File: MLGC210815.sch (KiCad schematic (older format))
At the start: 108 parts, among them J1 PinStrip_01x06_Male, J2 USB-B-04PFHTW, Q1 P-MOSFET_SI2315BDS-T1-E3, Q2 NPN_BC817, Q3 NPN_BC817, Q4 P-MOSFET_SI2315BDS-T1-E3, SW1 Switch-Tact_OMRON-B3F-3100, SW2 Switch-Tact_OMRON-B3F-3100, SW3 Switch-Tact_OMRON-B3F-3100, U1 PIC32MX170F256B-ISS, U2 OPA_MCP6V36T-E_OT, U3 LDO-MCP1700T-3302E_TT-Others, U4 SENSOR_BMA250E, U5 INTERFACE_FT230XS, U6 BATTERY_MCP73833-FCI_UN, U7 DISPLAY_REX012832FSPP3N01, Y1 Crystal_HC49SM_8MHz

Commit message: update
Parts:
- removed C14: Capacitator_0603_47nF_X7R, Passive:C_0603, symbol Passive:Capacitator_0603_47nF_X7R
- removed R16: Resistor_0603_4K70, Passive:R_0603, symbol Passive:Resistor_0603_4K70
- removed R17: Resistor_0603_9K10, Passive:R_0603, symbol Passive:Resistor_0603_9K10
- removed R18: Resistor_0603_10R0, Passive:R_0603, symbol Passive:Resistor_0603_10R0
- removed R44: Resistor_0603_0R00, Passive:R_0603, symbol Passive:Resistor_0603_0R00
- removed Y1: Crystal_HC49SM_8MHz, Passive:Crystal_SMD_HC49-SD, symbol Passive:Crystal_HC49SM_8MHz
- added J3, J4: PinHeader_01x01_Male, Connectors:PinHeader_1x01_P2.54mm_Horizontal, symbol Connectors:PinHeader_01x01_Male
- added J5: PinHeader_01x02_Male, Connectors:PinHeader_1x02_P2.54mm_Vertical, symbol Connectors:PinHeader_01x02_Male
- added L3: Filter_0603_CB03YTYH101, Passive:L_0603, symbol Passive:Filter_0603_CB03YTYH101
- added R44: Resistor_0603_220R, Passive:R_0603, symbol Passive:Resistor_0603_220R
- added R45: Resistor_0603_1K00, Passive:R_0603, symbol Passive:Resistor_0603_1K00
- added R?: Resistor_0603_0R00, Passive:R_0603, symbol Passive:Resistor_0603_0R00
- added Y1: Crystal_SMD3225_12MHz, Passive:Crystal_SMD_3225, symbol Passive:Crystal_SMD3225_12MHz
- B1: value BATTERY_CELLEVIA-L402036-Others -> BATTERY_L402036; symbol MLGC210815-rescue:BATTERY_CELLEVIA-L402036-Others -> Others:BATTERY_L402036
- C1, C10, C11, C2, C6, C8: value Capacitator_0805_100nF_X7R -> Capacitator_0603_100nF_X7R; footprint Passive:C_0805 -> Passive:C_0603; symbol Passive:Capacitator_0805_100nF_X7R -> Passive:Capacitator_0603_100nF_X7R; ManufacturerPartNo CC0805KRX7R9BB104 -> CC0603KRX7R9BB104; Supplier FAR-3019949;LOM-82-01-25 -> LOM-82-03-47;TME-CC0603KRX7R9BB104;
- C12, C16, C26, C34, C35, C36, C9: value Capacitator_0805_1uF_X7R -> Capacitator_0603_1uF_X7R; symbol Passive:Capacitator_0805_1uF_X7R -> Passive:Capacitator_0603_1uF_X7R; ManufacturerPartNo CC0603KRX7R7BB105 -> CC0603KRX7R7BB105;
- C20, C21, C22: Comment 100nF -> 10nF
- C3: value Capacitator_0805_10uF_X5R -> Capacitator_0603_10uF_X5R; footprint Passive:C_0805 -> Passive:C_0603; symbol Passive:Capacitator_0805_10uF_X5R -> Passive:Capacitator_0603_10uF_X5R; Manufacturer SAMSUNG -> Murata; ManufacturerPartNo CL21A106KOQNNNG -> GRM188R61A106KE69D; Supplier LOM-82-08-32;TME-0805YD106KAT2A;TME-CL21A106KOQNNNG; FAR-12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 -> LOM-82-13-69;
- C4, C5: value Capacitator_0805_22pF_X7R -> Capacitator_0603_22pF_NP0; footprint Passive:C_0805 -> Passive:C_0603; symbol Passive:Capacitator_0805_22pF_X7R -> Passive:Capacitator_0603_22pF_NP0; Manufacturer SAMSUNG -> YAGEO; ManufacturerPartNo CL21C220JBANNNC -> CC0603JRNP09BN220;; Supplier LOM-82-09-18; -> LOM-82-02-18;
- J1: value PinStrip_01x06_Male -> PinHeader_01x06_Male; footprint Connectors:PinStrip_1x06_P2.54mm_Vertical -> Connectors:PinHeader_1x06_P2.54mm_Vertical; symbol Connectors:PinStrip_01x06_Male -> Connectors:PinHeader_01x06_Male; Comment PinStrip_01x06_Male -> PinHeader_01x06_Male
- L2: Comment BLM21A -> 1K00@100MHz
- R1, R12, R6: value Resistor_0805_470R -> Resistor_0603_470R; footprint Passive:R_0805 -> Passive:R_0603; symbol Passive:Resistor_0805_470R -> Passive:Resistor_0603_470R; Manufacturer Walsin -> VIKING; ManufacturerPartNo WR08X471JTL -> WR06X4700FTL; Supplier LOM-81-30-15; -> LOM-80-31-61;TME-CQ0603-470R-1% ;
- R10, R14, R36, R9: value Resistor_0805_10K0 -> Resistor_0603_10K0; footprint Passive:R_0805 -> Passive:R_0603; symbol Passive:Resistor_0805_10K0 -> Passive:Resistor_0603_10K0; Manufacturer Walsin -> ASJ; ManufacturerPartNo WR08X471JTL -> CR16-1002-FK; Supplier LOM-81-30-15; -> LOM-80-15-13;TME-CRCW060310K0FKTABC;
- R11: value Resistor_0805_R_DNP -> Resistor_0603_R_DNP; footprint Passive:R_0805 -> Passive:R_0603; symbol Passive:Resistor_0805_R_DNP -> Passive:Resistor_0603_R_DNP
- R13: value Resistor_0805_0R00 -> Resistor_0603_0R00; footprint Passive:R_0805 -> Passive:R_0603; symbol Passive:Resistor_0805_0R00 -> Passive:Resistor_0603_0R00; Manufacturer VIKING -> Yageo Corp.; ManufacturerPartNo CR-05JL7----0R 0.125W -> RC0603JR-100RL;; Supplier LOM-81-10-02; -> LOM-81-34-80;
- R19, R20, R21, R28, R38, R43: footprint Passive:R_0805 -> Passive:R_0603
- R2, R3, R4: value Resistor_0805_220R -> Resistor_0603_220R; footprint Passive:R_0805 -> Passive:R_0603; symbol Passive:Resistor_0805_220R -> Passive:Resistor_0603_220R; ManufacturerPartNo CR-05FL7--220R 0.125W -> CR-03FL7--220R 0.1W; Supplier LOM-80-10-78; -> LOM-80-11-55;
- R5: value Resistor_0805_4K70 -> Resistor_0603_4K70; footprint Passive:R_0805 -> Passive:R_0603; symbol Passive:Resistor_0805_4K70 -> Passive:Resistor_0603_4K70; Manufacturer VIKING -> ROYAL OHM;; ManufacturerPartNo CR-05FL7---4K7 0.125W -> CQ0603-4K7-1%;; Supplier LOM-80-10-94 -> LOM-80-11-85;TME-CRCW06034K70FKEA;
- U3: value LDO-MCP1700T-3302E_TT-Others -> LDO_MCP1700T-3302E_TT; footprint Package_TO_SOT_SMD:SOT-23 -> Semiconductor:SOT-23; symbol MLGC210815-rescue:LDO-MCP1700T-3302E_TT-Others -> Others:LDO_MCP1700T-3302E_TT
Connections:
- net +3V3: now also U7.5 (VBAT)
- net +BATT: no longer U7.5 (VBAT)
- net 5V_USB: now also L3.1; no longer J2.1 (VBUS)
- net GNDD: now also J3.1 (Pin_1), J5.1 (Pin_1), Y1.2, Y1.4
- net at C5.1, U1.10 (OSC2): now also Y1.3
- net at C4.1, U1.9 (OSC1): now also Y1.1
- net at F1.2: now also J5.2 (Pin_2); no longer B1.1 (VBAT+)
- net at R15.1, U2.1: now also R?.1; no longer U2.4 (-)
- net at C8.2, R7.2: now also J4.1 (Pin_1)
- net #CH_CPLT renamed CH_CPLT#
- net #DEN renamed DEN#
- net #MCLR renamed MCLR#
- net #PG: no longer names the net of Q3.1 (B), R14.2
- net #PG: now also R45.2; no longer U6.7 (PG#)
- net #PSEN renamed PSEN#
- net #RST: no longer names the net of U7.9 (RES#)
- net #RST: now also R44.2; no longer U1.16 (RB7)
- net DWN renamed DN#
- net OK renamed OK#
- net UP renamed UP#
- new net: J2.1 (VBUS), L3.2
- new net: R?.2, U2.4 (-)
- new net PG#: R45.1, U6.7 (PG#)
- new net RST#: R44.1, U1.16 (RB7)
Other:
- note added: "Battery"
- moved on the sheet: C25, C26, C27, C31, C33, C34, D4, D5, D6, F1, R26, R27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

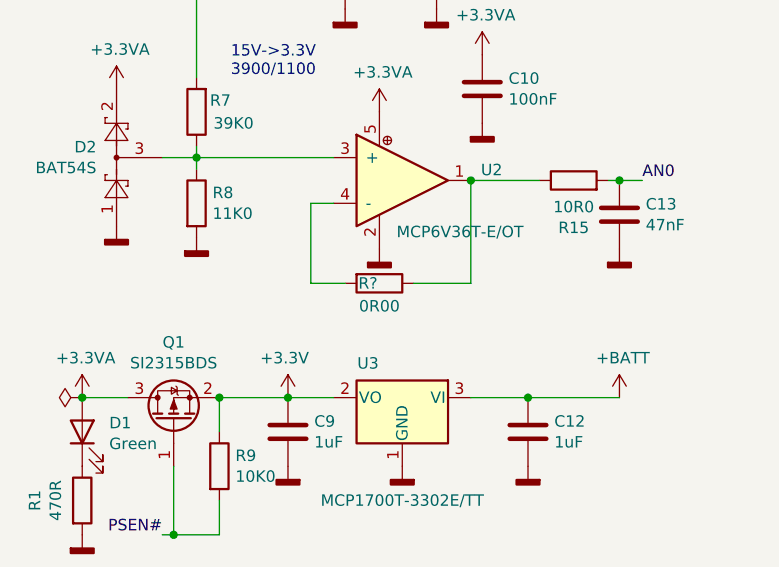
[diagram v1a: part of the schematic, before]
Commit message: remove doc files
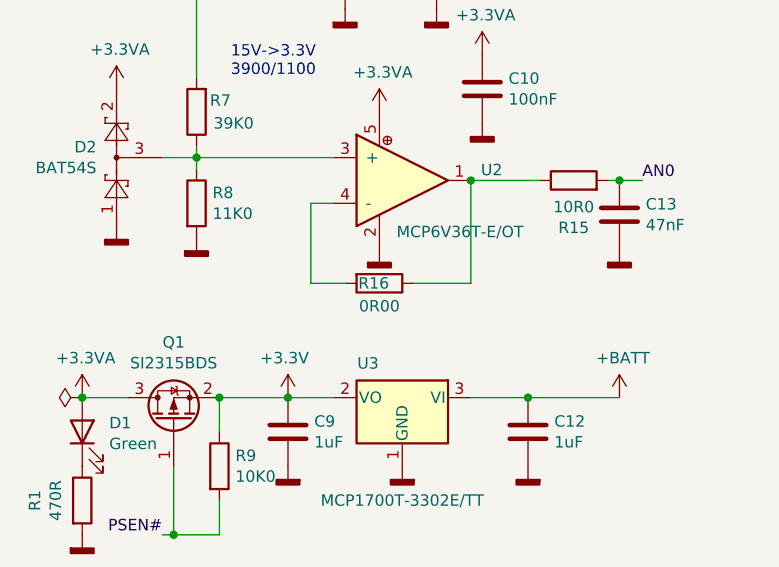
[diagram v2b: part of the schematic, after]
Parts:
- gave numbers to parts that had none: 1
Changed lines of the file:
@@
 $EndComp
 $Comp
-L Passive:Resistor_0603_0R00 R?
+L Passive:Resistor_0603_0R00 R16
 U 1 1 62325F14
 P 2050 6600
-F 0 "R?" V 2050 6550 50  0000 C CNN
+F 0 "R16" V 2050 6575 50  0000 C CNN
 F 1 "Resistor_0603_0R00" H 2100 6325 50  0001 C CNN
 F 2 "Passive:R_0603" H 2075 6250 50  0001 C CNN

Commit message: update
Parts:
- C20, C21, C22: Comment 10nF -> 1nF
- U7: value DISPLAY_REX012832FSPP3N01 -> DISPLAY_REX012832FWPP3N01; symbol Others:DISPLAY_REX012832FSPP3N01 -> Others:DISPLAY_REX012832FWPP3N01; Comment REX012832FSPP3N01 -> REX012832FWPP3N01; ManufacturerPartNo REX012832FSPP3N01 -> REX012832FWPP3N00001; Supplier TME-REX012832FSPP3N01 -> TME-REX012832FWPP3N01
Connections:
- net +3V3: no longer U7.5 (VBAT)
- net GNDD: now also U4.4 (GND)
- net at C29.1, Q4.3 (D): now also U7.5 (VBAT); no longer U7.6 (NC)
- no-connect marks 7 -> 10
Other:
- note added: "BOM OK"
- note added: "PCB OK"
- note added: "SCH OK"
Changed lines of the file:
@@
 $EndComp
 $Comp
-L Others:DISPLAY_REX012832FSPP3N01 U7
+L Others:DISPLAY_REX012832FWPP3N01 U7
 U 1 1 612FBC0E
 P 10150 1000
 F 0 "U7" H 9450 1400 50  0000 L CNN
-F 1 "DISPLAY_REX012832FSPP3N01" H 10150 1400 50  0001 C CNN
+F 1 "DISPLAY_REX012832FWPP3N01" H 10150 1400 50  0001 C CNN
 F 2 "Others:RAYSTAR_REX012832" H 10150 1400 50  0001 C CNN
-F 3 "${KNV_DATASHEET}\\RAYSTAR REX012832FSPP3N01.pdf" H 10150 1400 50  0001 C CNN
-F 4 "REX012832FSPP3N01" H 9450 1300 50  0000 L CNN "Comment"
+F 3 "${KNV_DATASHEET}\\RAYSTAR REX012832FWPP3N00001.pdf" H 10150 1400 50  0001 C CNN
+F 4 "REX012832FWPP3N01" H 9450 1300 50  0000 L CNN "Comment"
 F 5 "RAYSTAR OPTRONICS" H 10150 1400 50  0001 C CNN "Manufacturer"
-F 6 "REX012832FSPP3N01" H 10150 1400 50  0001 C CNN "ManufacturerPartNo"
-F 7 "TME-REX012832FSPP3N01" H 10150 1400 50  0001 C CNN "Supplier"
+F 6 "REX012832FWPP3N00001" H 10150 1400 50  0001 C CNN "ManufacturerPartNo"
+F 7 "TME-REX012832FWPP3N01" H 10150 1400 50  0001 C CNN "Supplier"
 	1    10150 1000
 	1    0    0    -1
@@
 U 1 1 6145A4D2
 P 8700 2200
-F 0 "R36" H 8770 2246 50  0000 L CNN
+F 0 "R36" V 8700 2125 50  0000 L CNN
 F 1 "Resistor_0603_10K0" H 8700 2200 50  0001 C CNN
 F 2 "Passive:R_0603" H 8700 2200 50  0001 C CNN
@@
 Wire Wire Line
 	9300 2000 9400 2000
-Wire Wire Line
-	10000 2000 10000 1400
 Text Label 8500 2350 2    50   ~ 0
 DEN#
@@
 Connection ~ 9400 2000
 Wire Wire Line
-	9400 2000 10000 2000
+	9400 2000 9900 2000
 $Comp
 L Passive:Capacitator_0603_2.2uF_X5R C28
@@
 F 2 "Passive:C_0603" H 5525 5750 50  0001 C CNN
 F 3 "" H 5550 6100 50  0001 C CNN
-F 4 "10nF" H 5665 6055 50  0000 L CNN "Comment"
+F 4 "1nF" H 5665 6055 50  0000 L CNN "Comment"
 F 5 "YAGEO;" H 5550 5600 50  0001 C CNN "Manufacturer"
 F 6 "CC0603JRNP09BN102;" H 5550 5525 50  0001 C CNN "ManufacturerPartNo"
@@
 F 2 "Passive:C_0603" H 5525 6900 50  0001 C CNN
 F 3 "" H 5550 7250 50  0001 C CNN
-F 4 "10nF" H 5665 7205 50  0000 L CNN "Comment"
+F 4 "1nF" H 5665 7205 50  0000 L CNN "Comment"
 F 5 "YAGEO;" H 5550 6750 50  0001 C CNN "Manufacturer"
 F 6 "CC0603JRNP09BN102;" H 5550 6675 50  0001 C CNN "ManufacturerPartNo"
@@
 F 2 "Passive:C_0603" H 5525 4500 50  0001 C CNN
 F 3 "" H 5550 4850 50  0001 C CNN
-F 4 "10nF" H 5665 4805 50  0000 L CNN "Comment"
+F 4 "1nF" H 5665 4805 50  0000 L CNN "Comment"
 F 5 "YAGEO;" H 5550 4350 50  0001 C CNN "Manufacturer"
 F 6 "CC0603JRNP09BN102;" H 5550 4275 50  0001 C CNN "ManufacturerPartNo"
@@
 U 1 1 613E244E
 P 7450 6000
-F 0 "R30" V 7650 6000 50  0000 C CNN
+F 0 "R30" V 7450 6000 50  0000 C CNN
 F 1 "Resistor_0603_0R00" H 7500 5725 50  0001 C CNN
 F 2 "Passive:R_0603" H 7475 5650 50  0001 C CNN
@@
 U 1 1 6146ED81
 P 7200 6250
-F 0 "R29" H 7270 6296 50  0000 L CNN
+F 0 "R29" V 7200 6175 50  0000 L CNN
 F 1 "Resistor_0603_R_DNP" H 7225 5975 50  0001 C CNN
 F 2 "Passive:R_0603" H 7225 5900 50  0001 C CNN
@@
 U 1 1 61309516
 P 2150 6150
-F 0 "U2" H 2494 6196 50  0000 L CNN
+F 0 "U2" H 2025 6150 50  0000 L CNN
 F 1 "OPA_MCP6V36T-E_OT" H 2100 6000 50  0001 C CNN
 F 2 "Semiconductor:SOT-23-5" H 2100 6000 50  0001 C CNN
 F 3 "${KNV_DATASHEET}\\MICROCHIP MCP6V36.pdf" H 2100 6000 50  0001 C CNN
 F 4 "MICROCHIP " H 2100 6000 50  0001 C CNN "Manufacturer"
-F 5 "MCP6V36T-E/OT" H 2125 5925 50  0000 L CNN "Comment"
+F 5 "MCP6V36T-E/OT" H 2375 5625 50  0000 L CNN "Comment"
 F 6 "MCP6V36T-E/OT" H 2100 6000 50  0001 C CNN "ManufacturerPartNo"
 F 7 "CHP-MCP6V36T-E/OT, FAR-3232356" H 2050 6000 50  0001 C CNN "Supplier"
@@
 	6100 1550 5650 1550
 Wire Wire Line
-	6000 1750 6000 1350
-Wire Wire Line
 	6000 1350 6100 1350
 Wire Wire Line
@@
 U 1 1 61A125BD
 P 8150 1150
-F 0 "R32" V 7943 1150 50  0000 C CNN
+F 0 "R32" V 8150 1150 50  0000 C CNN
 F 1 "Resistor_0603_4K70" H 8200 875 50  0001 C CNN
 F 2 "Passive:R_0603" H 8175 800 50  0001 C CNN
@@
 U 1 1 61A13545
 P 8450 1150
-F 0 "R33" V 8243 1150 50  0000 C CNN
+F 0 "R33" V 8450 1150 50  0000 C CNN
 F 1 "Resistor_0603_4K70" H 8500 875 50  0001 C CNN
 F 2 "Passive:R_0603" H 8475 800 50  0001 C CNN
@@
 	0    1    1    0
 $EndComp
-Wire Wire Line
-	9900 1400 9900 1750
-Wire Wire Line
-	9900 1750 10200 1750
-Connection ~ 10200 1750
 $Comp
 L Passive:Filter_0805_BLM21A102SPT L2
@@
 Wire Wire Line
 	2200 6600 2450 6600
+Text Notes 2975 1075 0    50   ~ 10
+SCH OK
+Text Notes 550  1150 0    50   ~ 10
+SCH OK
+Text Notes 2975 1000 0    50   ~ 10
+PCB OK
+Text Notes 2975 925  0    50   ~ 10
+BOM OK
+Text Notes 2375 6775 0    50   ~ 10
+SCH OK
+Text Notes 2375 6825 0    50   ~ 10
+PCB OK
+Text Notes 2375 6900 0    50   ~ 10
+BOM OK
+Text Notes 1750 7675 0    50   ~ 10
+SCH OK
+Text Notes 1775 7725 0    50   ~ 10
+PCB OK
+Text Notes 8825 5025 0    50   ~ 10
+SCH OK
+Text Notes 8825 5100 0    50   ~ 10
+PCB OK
+Text Notes 8825 4950 0    50   ~ 10
+BOM OK
+Text Notes 7825 2950 0    50   ~ 10
+SCH OK
+Text Notes 7825 3025 0    50   ~ 10
+PCB OK
+Wire Wire Line
+	9900 1400 9900 2000
+NoConn ~ 10000 1400
+NoConn ~ 10575 1875
+Text Notes 9650 625  0    50   ~ 10
+SCH OK
+NoConn ~ 10050 500
+Text Notes 9650 550  0    50   ~ 10
+PCB OK
+Text Notes 9650 475  0    50   ~ 10
+BOM OK
+Wire Wire Line
+	6000 1650 6100 1650
+Wire Wire Line
+	6000 1750 6000 1650
+Wire Wire Line
+	6000 1650 6000 1350
+Connection ~ 6000 1650
+Text Notes 6350 850  0    50   ~ 10
+SCH OK
+Text Notes 6350 750  0    50   ~ 10
+PCB OK
+$Comp
+L power:PWR_FLAG #FLG01
+U 1 1 617B062B
+P 9400 2000
+F 0 "#FLG01" H 9400 2075 50  0001 C CNN
+F 1 "PWR_FLAG" H 9400 2173 50  0001 C CNN
+F 2 "" H 9400 2000 50  0001 C CNN
+F 3 "~" H 9400 2000 50  0001 C CNN
+	1    9400 2000
+	1    0    0    -1
+$EndComp
 $EndSCHEMATC
